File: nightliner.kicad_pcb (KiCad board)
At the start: 2 copper layers, 154.8 x 116.1 mm, 81 parts, among them J1 TYPE-C-31-M-12, J2 Battery, P1 ISP_Prog, SW1 pinky_top, SW10 inner_home, SW11 pinky_bottom, SW12 ring_bottom, SW13 middle_bottom, SW14 index_bottom, SW15 inner_bottom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

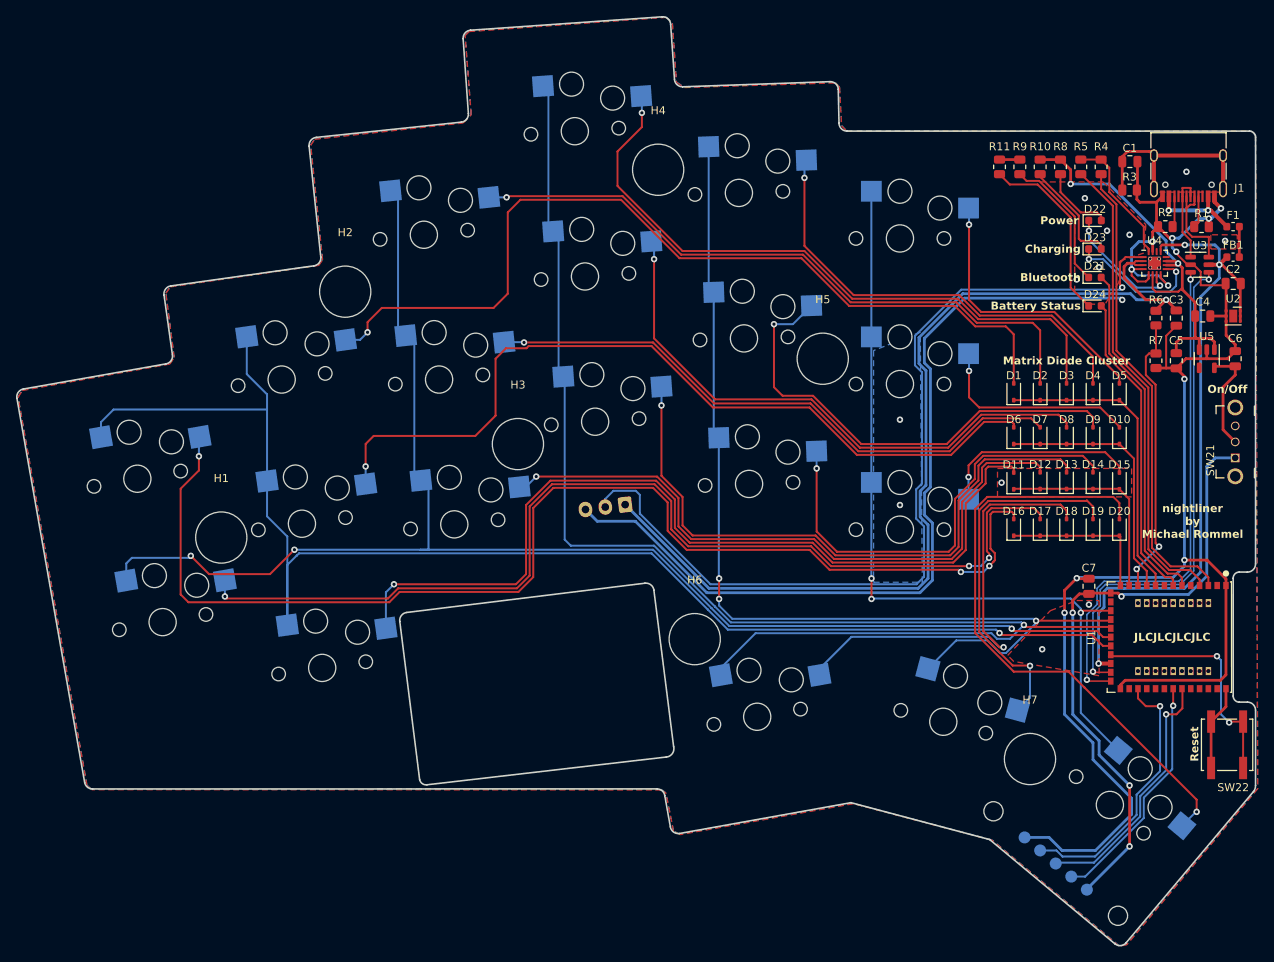
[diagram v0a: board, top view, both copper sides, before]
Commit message: feat: case for the keyboard
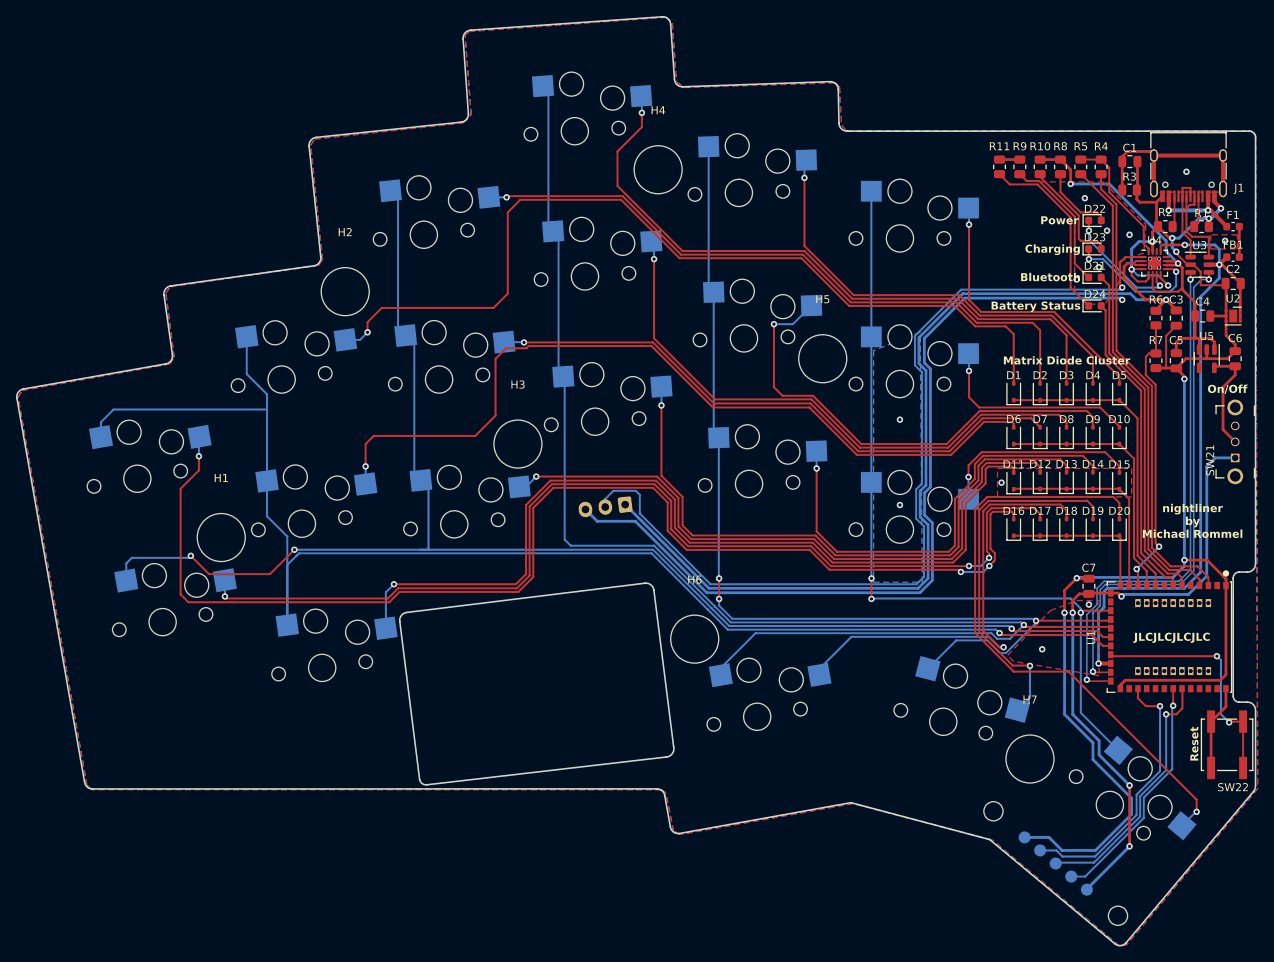
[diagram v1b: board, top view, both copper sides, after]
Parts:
- H1: value MountingHole_M3 -> Standoff_6mm_M3; footprint MountingHole:MountingHole_6.4mm_M6 -> miro_keyboard:StandOff_6mm_M3
- H2, H3, H4, H5, H6, H7: footprint MountingHole:MountingHole_6.4mm_M6 -> miro_keyboard:StandOff_6mm_M3

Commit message: fix: move battery connector to top
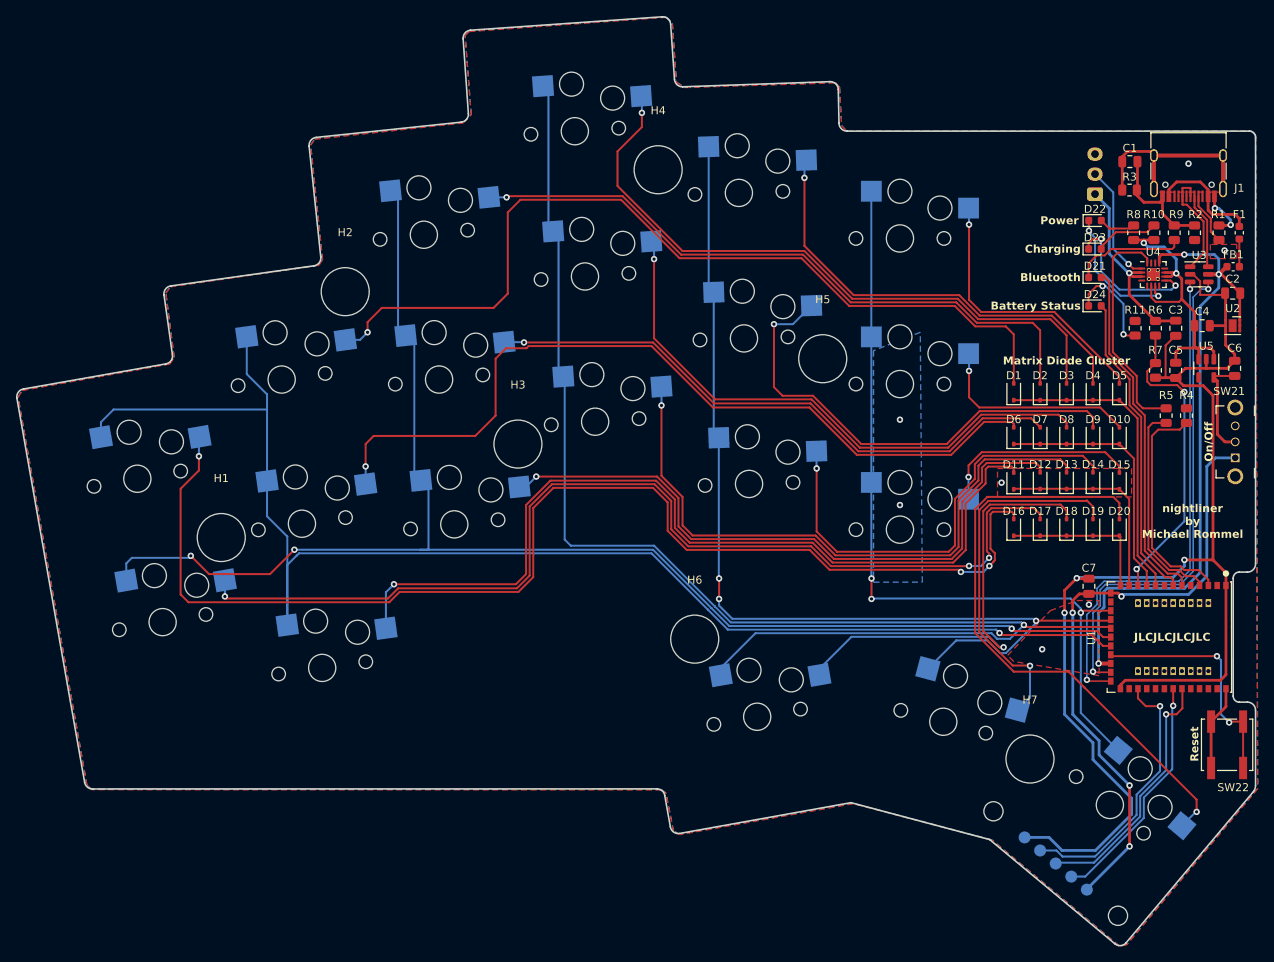
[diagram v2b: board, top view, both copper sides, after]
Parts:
- moved J2 70.4 mm to (153.4, 45.5), turned to 90 degrees
- moved R4 32.9 mm to (164.8, 73.2)
- moved R5 32.9 mm to (162.3, 73.2)
- moved R11 26.3 mm to (158.4, 62.2)
- moved R9 21.0 mm to (163.3, 50.3)
- moved R10 16.4 mm to (160.8, 50.3), turned to -90 degrees
- moved R8 12.3 mm to (158.2, 50.3), turned to -90 degrees
- moved R2 3.74 mm to (165.9, 50.3), turned to 90 degrees
- moved R1 2.31 mm to (168.9, 50.3), turned to 90 degrees
- moved U4 1.44 mm to (160.7, 55.5)
- moved C3 1.27 mm to (163.5, 62.2)
- moved R6 1.27 mm to (161.0, 62.2)
- moved C5 1.21 mm to (163.5, 67.5)
- moved R7 1.21 mm to (161.0, 67.5)
- moved U3 1.21 mm to (166.4, 55.5)
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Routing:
- net GND: track 327.9 -> 191.6 mm, vias 24 -> 12
- net /BAT_TEMP: track 113.9 -> 14.9 mm
- net /VBAT: track 122.9 -> 24.9 mm
- net CHARGE_CTRL_2: track 59.1 -> 26.2 mm
- net CHARGE_CTRL_1: track 58.9 -> 28.4 mm
- net VIN: track 52.6 -> 37.2 mm
- net Net-(U4-ISET): track 16.5 -> 28.7 mm
- net Net-(D24-K): track 23.1 -> 12.5 mm, vias 0 -> 2
- net Net-(D23-A): track 13.7 -> 7.97 mm
- net Net-(D22-A): track 9.14 -> 4.66 mm
- net Net-(J1-CC2): track 3.89 -> 0.00 mm
- net Net-(D21-K): track 17.4 -> 14.2 mm
- net /DPlus: track 11.1 -> 14.0 mm
- net Net-(F1-Pad1): track 11.7 -> 14.4 mm, vias 2 -> 0
- net VSENSE: track 35.5 -> 38.2 mm
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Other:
- outline, holes or cut-outs redrawn

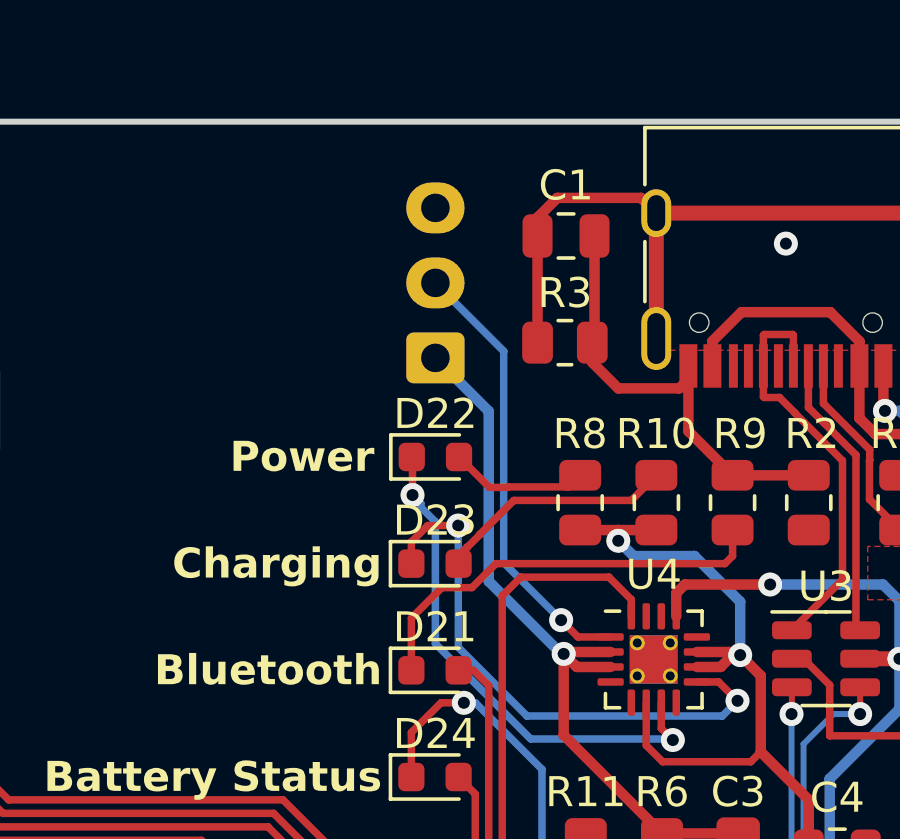
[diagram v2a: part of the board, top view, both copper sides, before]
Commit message: fix: add 0.2mm offset for case clearance
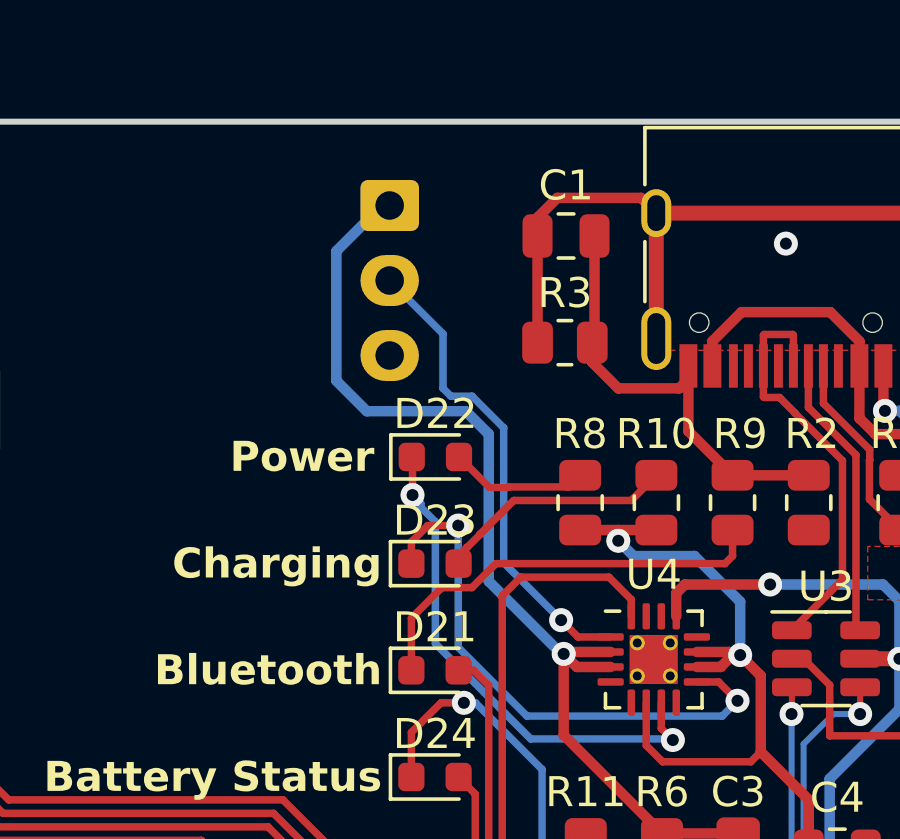
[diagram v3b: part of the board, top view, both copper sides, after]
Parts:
- moved J2 5.30 mm to (151.9, 40.4), turned to -90 degrees
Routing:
- net /VBAT: track 24.9 -> 34.2 mm
- net /BAT_TEMP: track 14.9 -> 16.0 mm

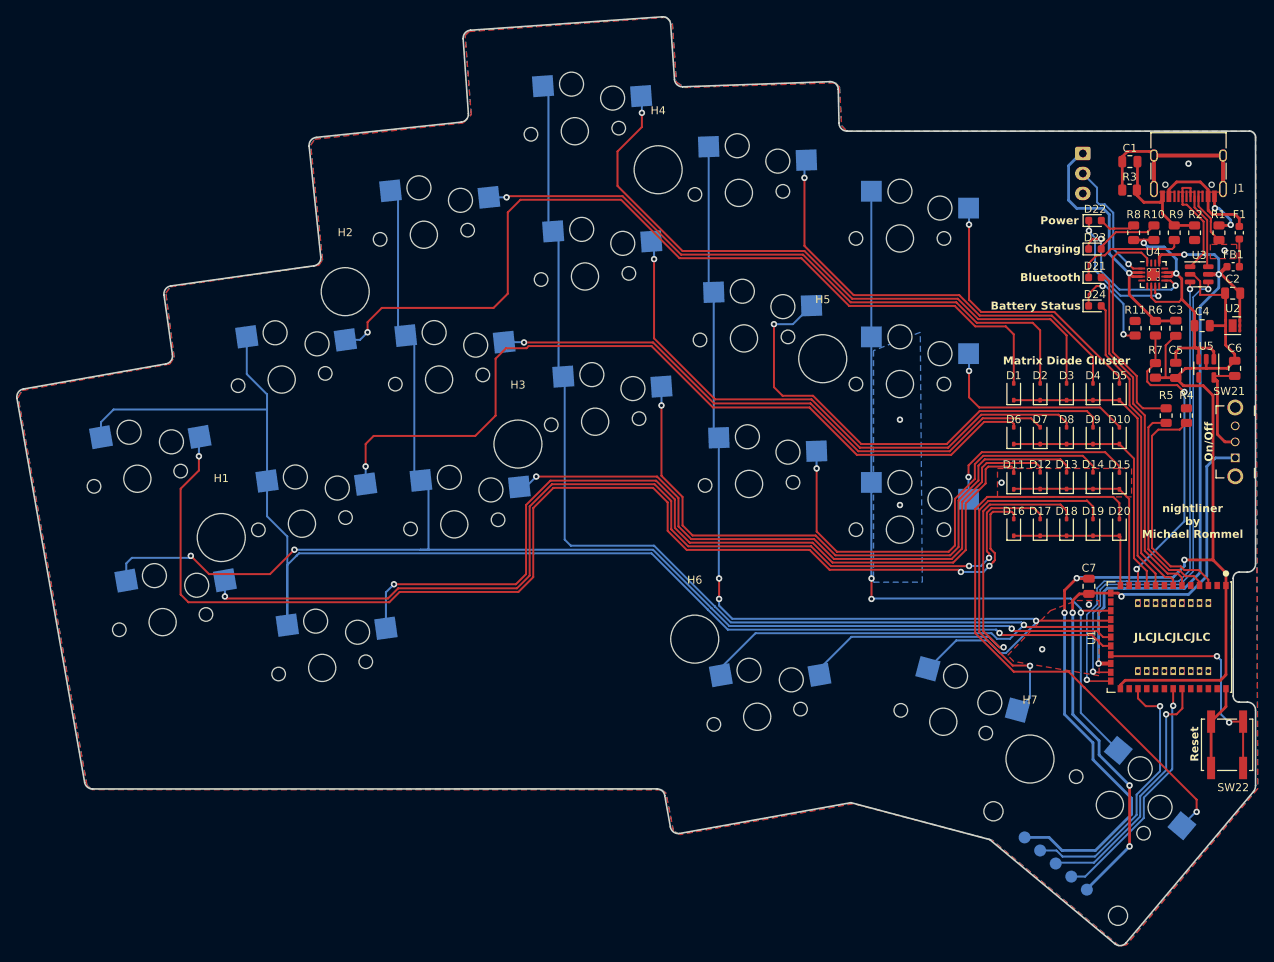
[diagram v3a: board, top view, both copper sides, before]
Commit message: feat: add split pogo connector, reroute board
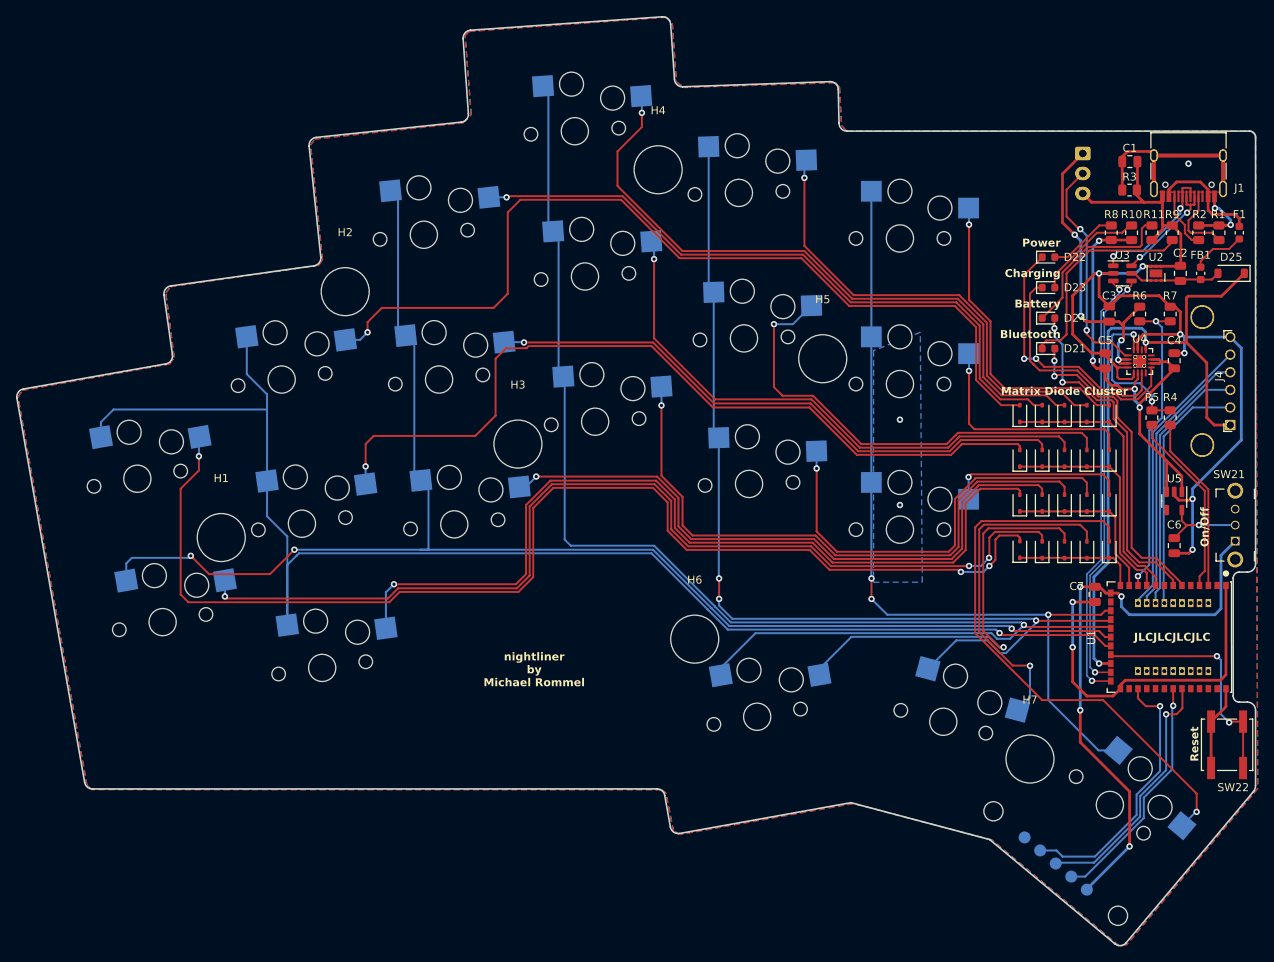
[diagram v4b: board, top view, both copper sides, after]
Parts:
- added D25: 1N5819W, Diode_SMD:D_SOD-123, F.Cu at (170.4, 55.4)
- added J4: Serial, miro_keyboard:MagConn_6pin_left, F.Cu at (170.3, 74.3)
- moved C6 23.4 mm to (163.3, 89.4), turned to -90 degrees
- moved U5 17.1 mm to (163.3, 83.8)
- moved R11 12.1 mm to (160.5, 50.3), turned to -90 degrees
- moved U2 11.6 mm to (161.0, 55.4), turned to -90 degrees
- moved U4 11.0 mm to (159.0, 66.4)
- moved D21 10.6 mm to (147.6, 64.8)
- moved SW21 10.4 mm to (170.9, 88.8)
- moved U3 9.60 mm to (156.8, 55.4)
- moved C5 8.91 mm to (154.7, 66.3), turned to 90 degrees
- moved C3 8.50 mm to (155.2, 60.5), turned to 90 degrees
- moved D23 7.55 mm to (147.6, 57.1)
- moved D22 7.40 mm to (147.6, 53.3)
- moved R7 7.28 mm to (162.8, 60.5), turned to 90 degrees
- moved C2 6.99 mm to (164.1, 55.4), turned to -90 degrees
- moved D24 6.00 mm to (147.6, 61.0)
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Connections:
- C2 pad 2: VBUS -> Net-(D25-A)
- FB1 pad 2: VBUS -> Net-(D25-A)
- U1 pad 19: unconnected-(U1-P0.27-Pad19) -> RX
- U1 pad 20: unconnected-(U1-P0.08-Pad20) -> TX
- U1 pad 21: unconnected-(U1-P0.06-Pad21) -> RTS
- U1 pad 22: unconnected-(U1-P0.26-Pad22) -> CTS
- U2 pad 4: VBUS -> Net-(D25-A)
- U2 pad 5: VBUS -> Net-(D25-A)
- U2 pad 6: VBUS -> Net-(D25-A)
- U3 pad 5: VBUS -> Net-(D25-A)
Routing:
- net CTS: track 0.00 -> 35.8 mm
- net RTS: track 0.00 -> 34.1 mm
- net TX: track 0.00 -> 32.4 mm
- net RX: track 0.00 -> 30.7 mm
- net VIN: track 37.2 -> 60.1 mm, vias 2 -> 4
- net Net-(D22-K): track 17.2 -> 32.7 mm
- net Net-(D21-K): track 14.2 -> 26.9 mm
- net /BAT_TEMP: track 16.0 -> 28.3 mm, vias 1 -> 2
- net Net-(D23-K): track 18.7 -> 30.4 mm, vias 2 -> 0
- net Net-(D25-A): track 0.00 -> 11.6 mm
- net D-: track 62.9 -> 53.3 mm
- net Net-(D24-K): track 12.5 -> 21.6 mm, vias 2 -> 0
- net D+: track 63.6 -> 54.6 mm
- net Net-(U4-ISET): track 28.7 -> 20.2 mm, vias 0 -> 2
- net Net-(J1-CC2): track 0.00 -> 7.71 mm
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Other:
- board text added: "Battery"
- board text removed: "Battery Status"
- board text removed: "LiPo Battery (30mm x 20mm)"
